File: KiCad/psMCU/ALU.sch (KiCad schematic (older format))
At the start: 20 parts

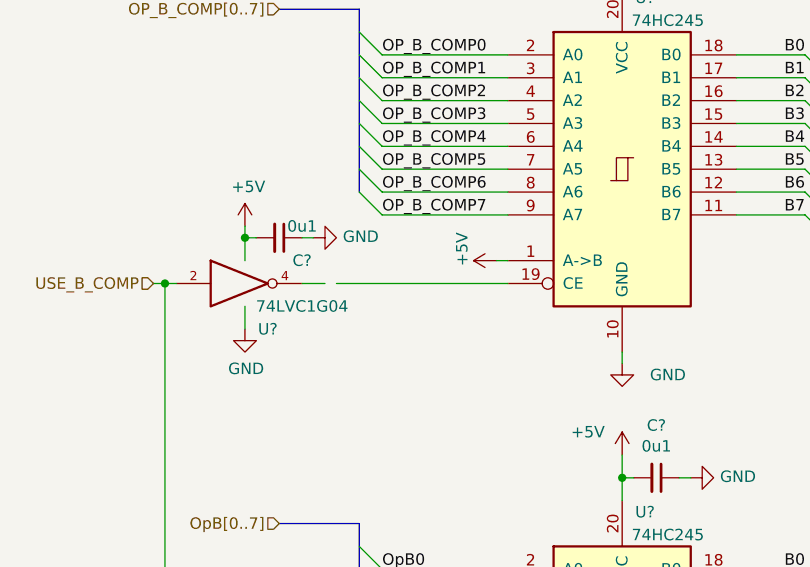
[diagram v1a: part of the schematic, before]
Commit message: First ERC pass
    All unconnects solved, need to inspect Tristate errors.
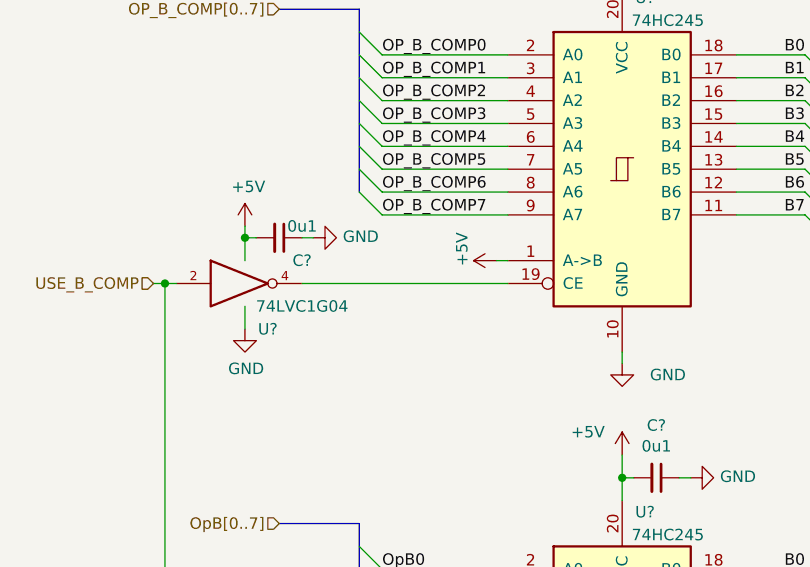
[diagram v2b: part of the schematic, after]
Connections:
- net at U?.19 (CE): now also U?.4
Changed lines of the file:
@@
 $Descr A4 11693 8268
 encoding utf-8
-Sheet 167 209
+Sheet 96 207
 Title "psMCU"
 Date ""
@@
 Wire Wire Line
 	1500 4350 1500 4250
-Wire Wire Line
-	1850 4150 1750 4150
 Entry Wire Line
 	2000 3050 2100 3150
@@
 	2000 5200 1650 5200
 Wire Wire Line
-	1900 4150 2650 4150
-Wire Wire Line
 	1100 4150 1150 4150
 Wire Wire Line
@@
 Wire Wire Line
 	1150 6400 2650 6400
+Wire Wire Line
+	1750 4150 2650 4150
 Wire Bus Line
 	4750 1750 4750 4450

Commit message: Added some footprints, small optimisations
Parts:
- U? (x4): footprint (none) -> Package_TO_SOT_SMD:SOT-353_SC-70-5
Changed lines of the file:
@@
 F 0 "U?" H 7250 2400 50  0000 C CNN
 F 1 "74LVC1G04" H 7400 2500 50  0000 C CNN
-F 2 "" H 7150 2600 50  0001 C CNN
+F 2 "Package_TO_SOT_SMD:SOT-353_SC-70-5" H 7150 2600 50  0001 C CNN
 F 3 "http://www.ti.com/lit/sg/scyt129e/scyt129e.pdf" H 7150 2600 50  0001 C CNN
 	1    7150 2600
@@
 F 0 "U?" H 7050 4900 50  0000 C CNN
 F 1 "74LVC1G04" H 7200 5000 50  0000 C CNN
-F 2 "" H 6950 5100 50  0001 C CNN
+F 2 "Package_TO_SOT_SMD:SOT-353_SC-70-5" H 6950 5100 50  0001 C CNN
 F 3 "http://www.ti.com/lit/sg/scyt129e/scyt129e.pdf" H 6950 5100 50  0001 C CNN
 	1    6950 5100
@@
 F 0 "U?" H 9400 4250 50  0000 C CNN
 F 1 "74LVC1G04" H 9550 4350 50  0000 C CNN
-F 2 "" H 9300 4450 50  0001 C CNN
+F 2 "Package_TO_SOT_SMD:SOT-353_SC-70-5" H 9300 4450 50  0001 C CNN
 F 3 "http://www.ti.com/lit/sg/scyt129e/scyt129e.pdf" H 9300 4450 50  0001 C CNN
 	1    9300 4450
@@
 F 0 "U?" H 1600 3950 50  0000 C CNN
 F 1 "74LVC1G04" H 1750 4050 50  0000 C CNN
-F 2 "" H 1500 4150 50  0001 C CNN
+F 2 "Package_TO_SOT_SMD:SOT-353_SC-70-5" H 1500 4150 50  0001 C CNN
 F 3 "http://www.ti.com/lit/sg/scyt129e/scyt129e.pdf" H 1500 4150 50  0001 C CNN
 	1    1500 4150

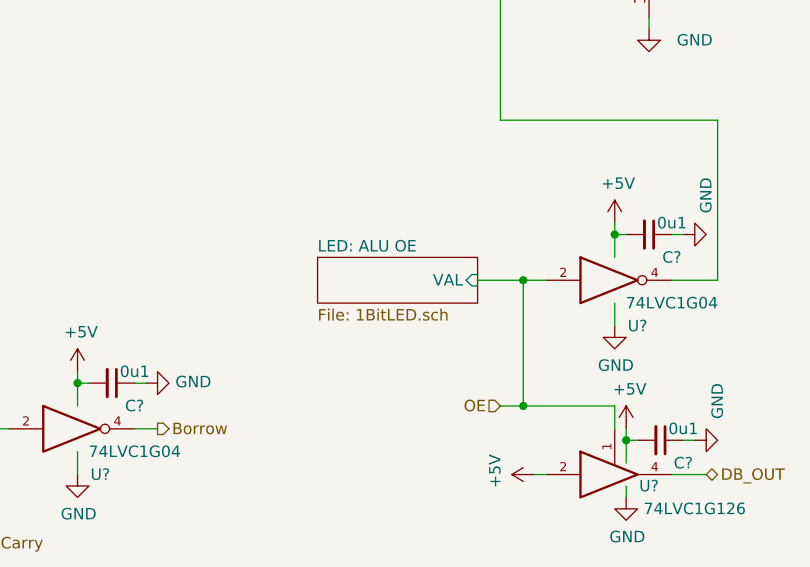
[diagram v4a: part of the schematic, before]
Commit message: Removed Single LED sheets
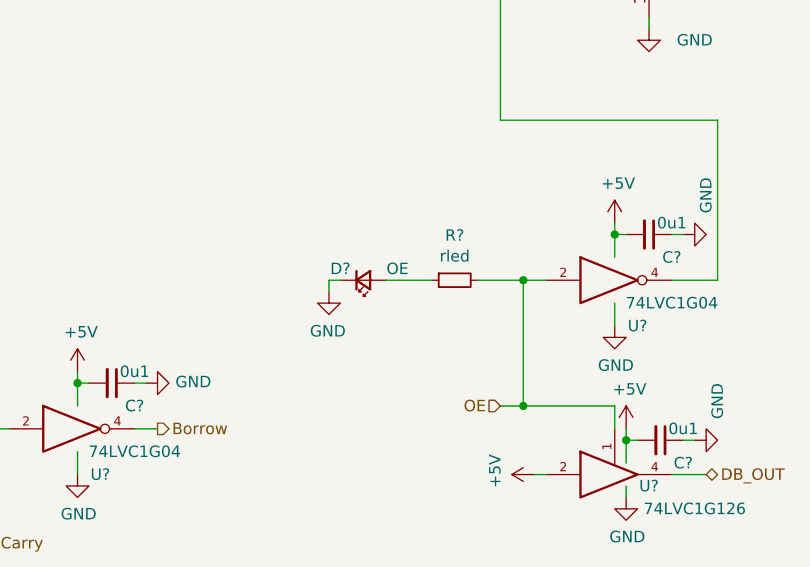
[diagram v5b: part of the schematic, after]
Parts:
- added D?: OE, Diode_SMD:D_0603_1608Metric, symbol Device:LED_Small
- added R?: rled, Resistor_SMD:R_0603_1608Metric, symbol Device:R_Small
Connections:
- net GND: now also D?.1 (K)
- net OE: now also R?.2
- new net: D?.2 (A), R?.1

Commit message: First Schematic Draft done.
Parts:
- C195, C196, C197, C198, C199, C200, C201, C202, C203, C204: renamed from C?; footprint Capacitor_SMD:C_0603_1608Metric -> NoRef_Footprints:C_0603_1608Metric_NoRef
- D202: renamed from D?; footprint Diode_SMD:D_0603_1608Metric -> NoRef_Footprints:D_0603_1608Metric_NoRef
- R206: renamed from R?; footprint Resistor_SMD:R_0603_1608Metric -> NoRef_Footprints:R_0603_1608Metric
- gave numbers to parts that had none: 10
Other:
- note added: "ALU"
- note added: "Output"
- note added: "Select between Operand B and the \n2's complement of Operand B"
- moved on the sheet: C195, C196, C197, C198, C199, C200, C201, C202, C203, C204, D202, R206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

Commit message: Small improvements.
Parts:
- renumbered C195 to C193, C196 to C194, C197 to C195, C198 to C196, C199 to C197, C200 to C198, C201 to C199, C202 to C200, C203 to C201, C204 to C202, U195 to U193, U196 to U194, U197 to U195, U198 to U196, U199 to U197, U200 to U198, U201 to U199, U202 to U200, U203 to U201, U204 to U202
